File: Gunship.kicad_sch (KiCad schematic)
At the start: 26 parts

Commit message: Changes in led and motor configs
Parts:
- removed M3: (no value), symbol Motor:Motor_Servo
- added D?: GREEN LIGHT, symbol Device:LED
- added D?: (no value), symbol Device:LED
- added R? (x2): (no value), symbol Device:R
- A1: value (none) -> Arduino_UNO_R3; footprint (none) -> Module:Arduino_UNO_R3
- BT1, BT2: value (none) -> 3.6V 18650 cell
- D1, D4, D5: value (none) -> 1N4004; footprint (none) -> Diode_THT:D_DO-41_SOD81_P10.16mm_Horizontal
- M1: value (none) -> MAIN ROTOR
- M?: value (none) -> TAIL ROTOR
- Q1, Q2: value (none) -> 2N2222; footprint (none) -> Package_TO_SOT_THT:TO-92_Inline
- R1, R2: value (none) -> 10K
- R?: value 150 -> (none)
- renumbered M2 to M1
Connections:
- net VPP: now also R?.1, R?.1
- net REDPULSE: now reaches A1.26 (D11)
- net REDPULSE: now also D?.1 (K)
- net at D3.1 (K), Q2.1 (C): now also D?.1 (K)
- net at D3.2 (A): now also R?.2; no longer D2.1 (K)
- net GREENLIGHTS renamed CONSTANTLEDS
- net ServoX renamed GUNSERVO
- net ServoY: no longer names the net of A1.21 (D6)
- new net: D2.1 (K), D?.2 (A)
- new net: D?.2 (A), R?.2
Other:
- moved on the sheet: D2, D3, D?, J?, Q2, Q?, R2, R3, R?

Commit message: Adjusted single red power feed
Single red led is driven directly from the Arduino, and needs to be fed from +5V (VCC) and not the batteries (VPP).
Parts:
- D2: value (none) -> RED LED
- D3: value (none) -> WHITE LED
- D?: value (none) -> RED PULSE
- D?: value (none) -> PULSELEDS GREEN
- D?: value (none) -> PULSELEDS RED
- J?: value (none) -> MP3 player
- M1: value (none) -> GunServo
- R3, R?: value (none) -> 270
- R?: value (none) -> 390
- R?: value (none) -> 470
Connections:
- net VCC: now also R?.1
- net VPP: no longer R?.1
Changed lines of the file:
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@@
       (effects (font (size 1.27 1.27)) (justify right))
     )
-    (property "Value" "" (id 1) (at 170.6372 110.5408 90)
+    (property "Value" "WHITE LED" (id 1) (at 170.6372 110.5408 90)
       (effects (font (size 1.27 1.27)) (justify right))
     )
@@
       (effects (font (size 1.27 1.27)) (justify left))
     )
-    (property "Value" "" (id 1) (at 184.658 95.123 0)
+    (property "Value" "270" (id 1) (at 184.658 95.123 0)
       (effects (font (size 1.27 1.27)) (justify left))
     )
@@
       (effects (font (size 1.27 1.27)) (justify right))
     )
-    (property "Value" "" (id 1) (at 185.8772 102.9208 90)
+    (property "Value" "RED LED" (id 1) (at 185.8772 102.9208 90)
       (effects (font (size 1.27 1.27)) (justify right))
     )
@@
       (effects (font (size 1.27 1.27)) (justify left))
     )
-    (property "Value" "" (id 1) (at 164.6428 28.6004 0)
+    (property "Value" "GunServo" (id 1) (at 164.6428 28.6004 0)
       (effects (font (size 1.27 1.27)) (justify left))
     )
@@
       (effects (font (size 1.27 1.27)) (justify left))
     )
-    (property "Value" "" (id 1) (at 210.058 115.443 0)
+    (property "Value" "270" (id 1) (at 210.058 115.443 0)
       (effects (font (size 1.27 1.27)) (justify left))
     )
@@
       (effects (font (size 1.27 1.27)) (justify right))
     )
-    (property "Value" "" (id 1) (at 141.4272 160.0708 90)
+    (property "Value" "RED PULSE" (id 1) (at 141.4272 160.0708 90)
       (effects (font (size 1.27 1.27)) (justify right))
     )
@@
       (effects (font (size 1.27 1.27)) (justify left))
     )
-    (property "Value" "" (id 1) (at 167.132 69.0122 0)
+    (property "Value" "MP3 player" (id 1) (at 167.132 69.0122 0)
       (effects (font (size 1.27 1.27)) (justify left))
     )
@@
       (effects (font (size 1.27 1.27)) (justify left))
     )
-    (property "Value" "" (id 1) (at 169.418 95.123 0)
+    (property "Value" "390" (id 1) (at 169.418 95.123 0)
       (effects (font (size 1.27 1.27)) (justify left))
     )
@@
       (effects (font (size 1.27 1.27)) (justify right))
     )
-    (property "Value" "" (id 1) (at 211.2772 123.2408 90)
+    (property "Value" "PULSELEDS GREEN" (id 1) (at 211.2772 123.2408 90)
       (effects (font (size 1.27 1.27)) (justify right))
     )
@@
     (pin "3")
   )
-  (symbol (lib_id "power:VPP") (at 138.43 146.05 0) (unit 1)
-    (in_bom yes) (on_board yes)
-    (property "Reference" "#PWR?" (id 0) (at 138.43 149.86 0)
-      (effects (font (size 1.27 1.27)) hide)
-    )
-    (property "Value" "VPP" (id 1) (at 138.811 141.6558 0))
-    (property "Footprint" "" (id 2) (at 138.43 146.05 0)
-      (effects (font (size 1.27 1.27)) hide)
-    )
-    (property "Datasheet" "" (id 3) (at 138.43 146.05 0)
-      (effects (font (size 1.27 1.27)) hide)
-    )
-    (pin "1")
-  )
   (symbol (lib_id "power:VPP") (at 167.64 88.9 0) (unit 1)
     (in_bom yes) (on_board yes)
@@
     (pin "1")
   )
+  (symbol (lib_id "power:VCC") (at 138.43 146.05 0) (unit 1)
+    (in_bom yes) (on_board yes)
+    (property "Reference" "#PWR?" (id 0) (at 138.43 149.86 0)
+      (effects (font (size 1.27 1.27)) hide)
+    )
+    (property "Value" "VCC" (id 1) (at 138.811 141.6558 0))
+    (property "Footprint" "" (id 2) (at 138.43 146.05 0)
+      (effects (font (size 1.27 1.27)) hide)
+    )
+    (property "Datasheet" "" (id 3) (at 138.43 146.05 0)
+      (effects (font (size 1.27 1.27)) hide)
+    )
+    (pin "1")
+  )
   (symbol (lib_id "Diode:1N4004") (at 238.76 59.69 270) (unit 1)
     (in_bom yes) (on_board yes)
@@
       (effects (font (size 1.27 1.27)) (justify left))
     )
-    (property "Value" "" (id 1) (at 140.208 152.273 0)
+    (property "Value" "470" (id 1) (at 140.208 152.273 0)
       (effects (font (size 1.27 1.27)) (justify left))
     )
@@
       (effects (font (size 1.27 1.27)) (justify right))
     )
-    (property "Value" "" (id 1) (at 211.2772 130.8608 90)
+    (property "Value" "PULSELEDS RED" (id 1) (at 211.2772 130.8608 90)
       (effects (font (size 1.27 1.27)) (justify right))
     )
@@
       (reference "#PWR?") (unit 1) (value "VPP") (footprint "")
     )
-    (path "/ab79a2d8-9d16-447c-be02-a38a9d270d31"
-      (reference "#PWR?") (unit 1) (value "VPP") (footprint "")
-    )
     (path "/b0f6a260-595a-4dc3-b1cd-177aded0c324"
       (reference "#PWR?") (unit 1) (value "VPP") (footprint "")
     )
+    (path "/b9f7803b-2d1f-4d54-9314-0bb75d4d2a99"
+      (reference "#PWR?") (unit 1) (value "VCC") (footprint "")
+    )
     (path "/ec77f04f-e7dc-48eb-a482-9f432c28059a"

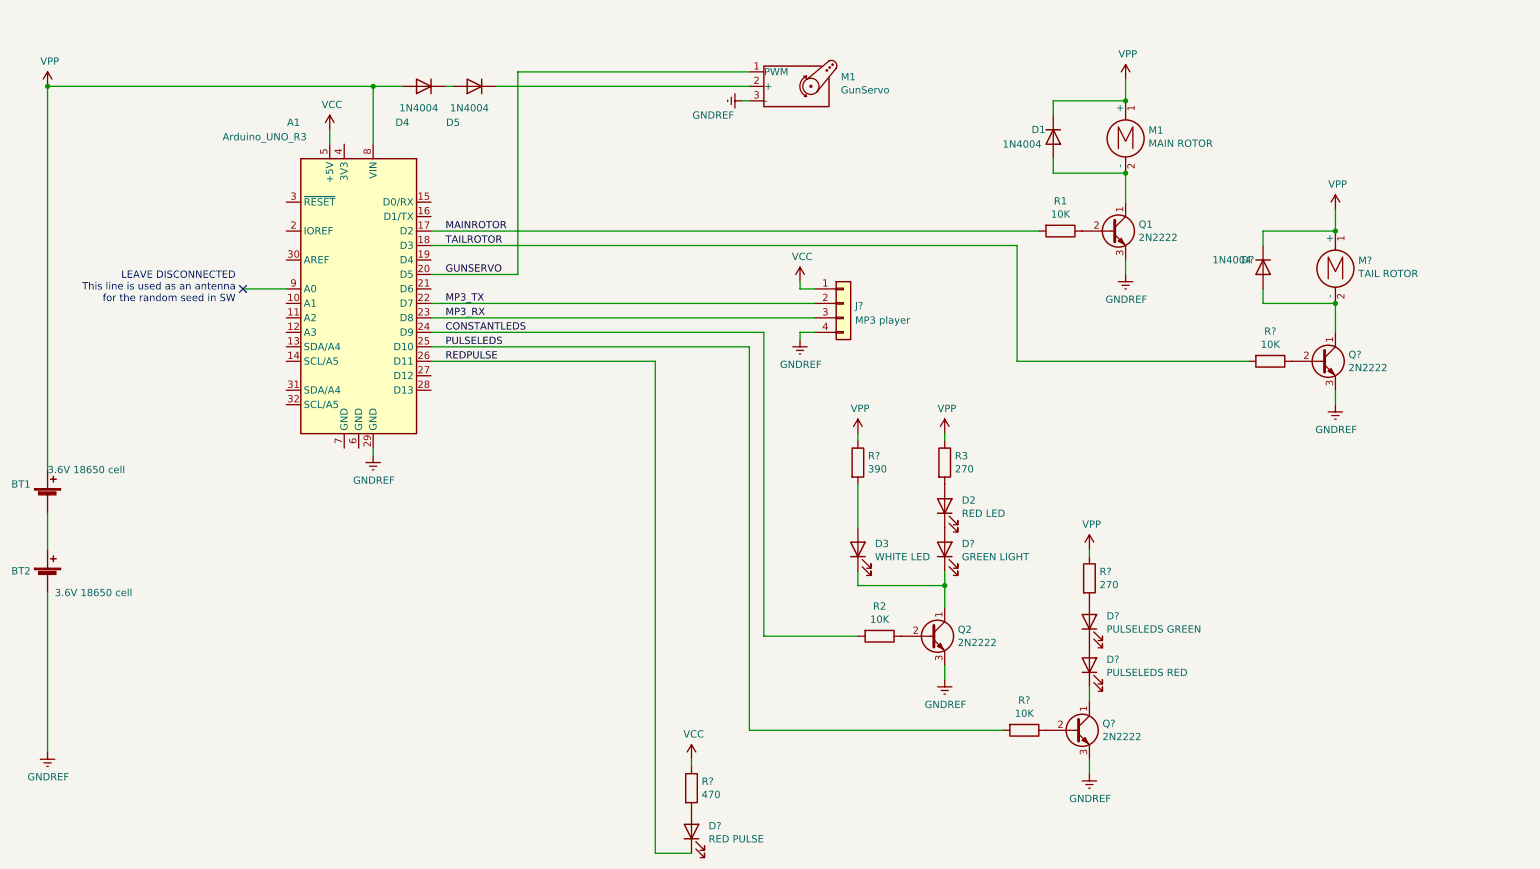
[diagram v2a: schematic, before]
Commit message: Hardware changes
Separate batteries for the DC motors and RED pulse led is now driven through a 2N2222 just like the rest
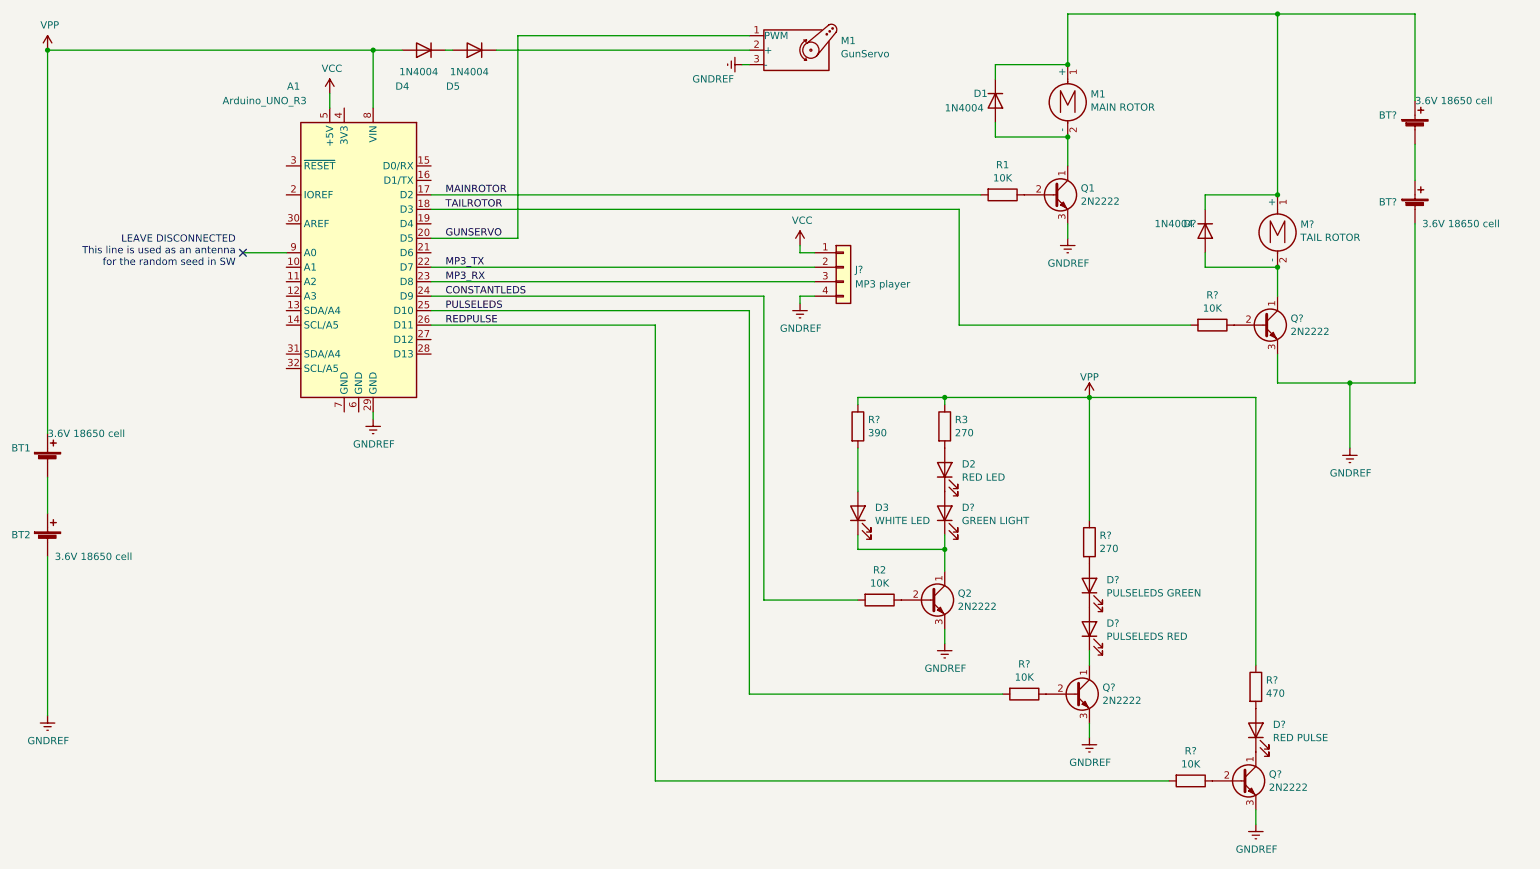
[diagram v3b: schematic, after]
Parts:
- added BT? (x2): 3.6V 18650 cell, symbol Device:Battery_Cell
- added Q?: 2N2222, Package_TO_SOT_THT:TO-92_Inline, symbol Transistor_BJT:BC547
- added R?: 10K, symbol Device:R
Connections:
- net GNDREF: now also BT?.2 (-), Q?.3 (E)
- net REDPULSE: now also R?.2; no longer D?.1 (K)
- net VCC: no longer R?.1
- net VPP: now also R?.1; no longer D1.1 (K), D?.1 (K), M1.1 (+), M?.1 (+)
- new net: BT?.1 (+), D1.1 (K), D?.1 (K), M1.1 (+), M?.1 (+)
- new net: D?.1 (K), Q?.1 (C)
- new net: Q?.2 (B), R?.1
- new net: BT?.1 (+), BT?.2 (-)
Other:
- moved on the sheet: A1, BT1, BT2, D1, D2, D3, D4, D5, D?, J?, M1, M?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
